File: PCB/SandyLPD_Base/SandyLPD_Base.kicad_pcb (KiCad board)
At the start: 2 copper layers, 270.8 x 100.7 mm, 292 parts, among them J1 Conn_02x02_Odd_Even, J10 Conn_01x10_Pin, J11 Conn_01x03, J12 Conn_01x01_Pin, J2 Conn_01x03, J3 Conn_01x01_Pin, J4 Conn_01x10_Pin, J5 USB_C_Receptacle_USB2.0, J6 USB_C_Receptacle_USB2.0, J7 USB_C_Receptacle_USB2.0, J8 USB_C_Receptacle_USB2.0, J9 Conn_02x02_Odd_Even, SW1 BOOT, SW2 BOOT_ALT, SW3 SW_DIP_x04, SW4 BOOT, SW5 BOOT_ALT, SW6 SW_DIP_x04, U1 NCP1117-3.3_SOT223, U2 NCP1117-3.3_SOT223, U3 RP2040, U4 W25Q128JVPIQ, U5 RP2040, U6 W25Q128JVPIQ, Y1 12MHz, Y2 12MHz

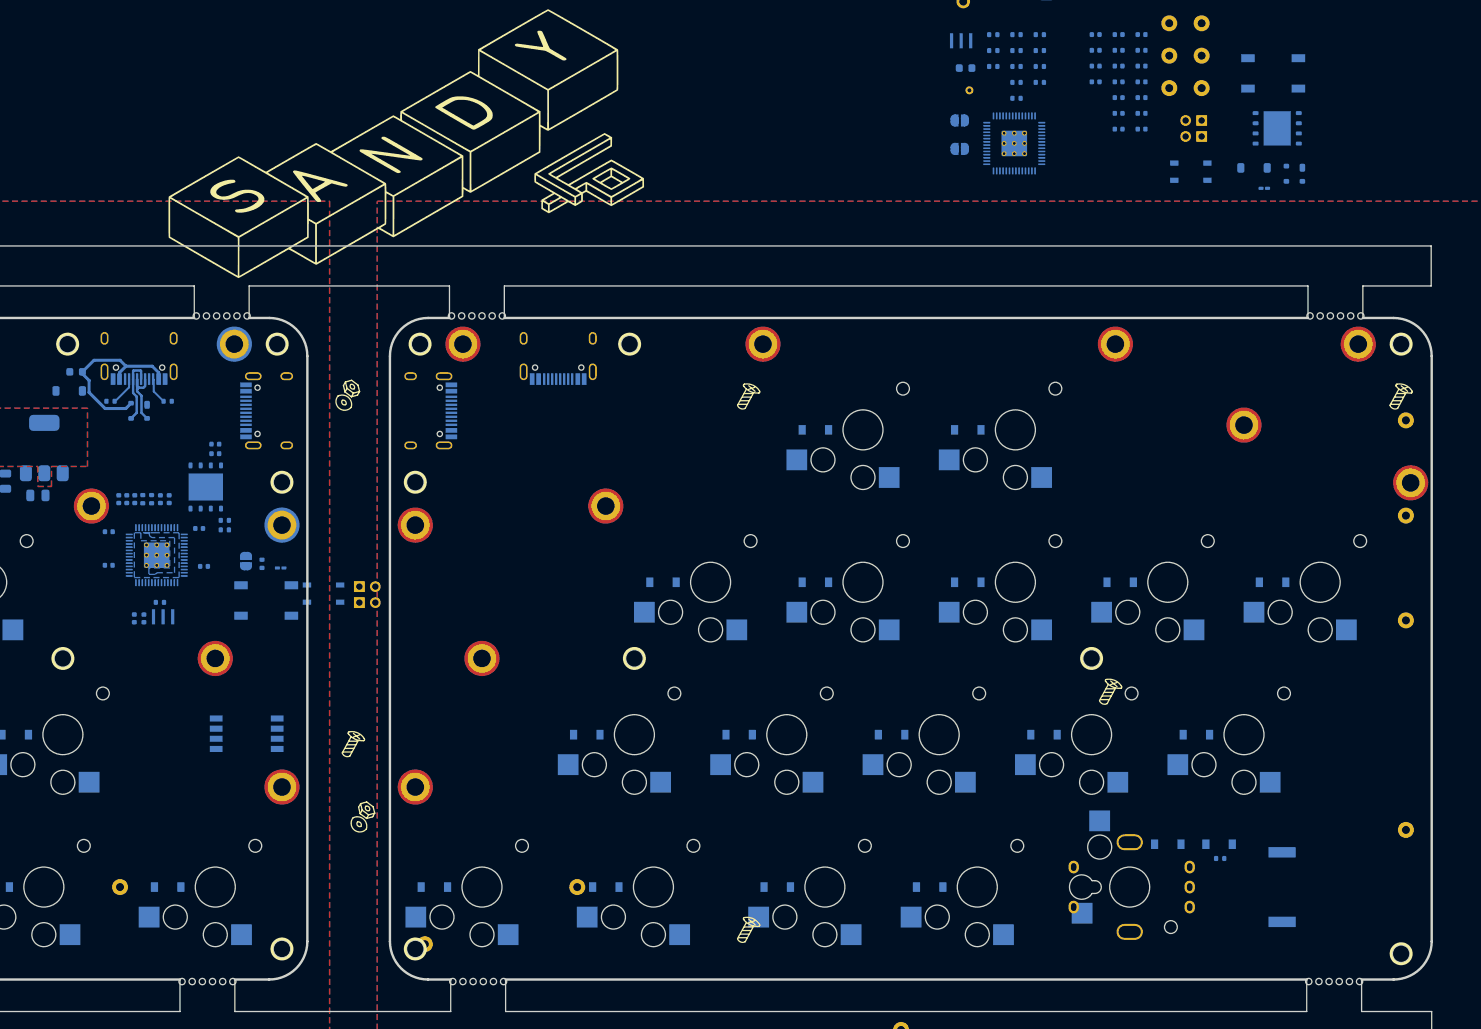
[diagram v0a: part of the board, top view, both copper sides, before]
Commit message: Base基板 MCUまわりの配置検討
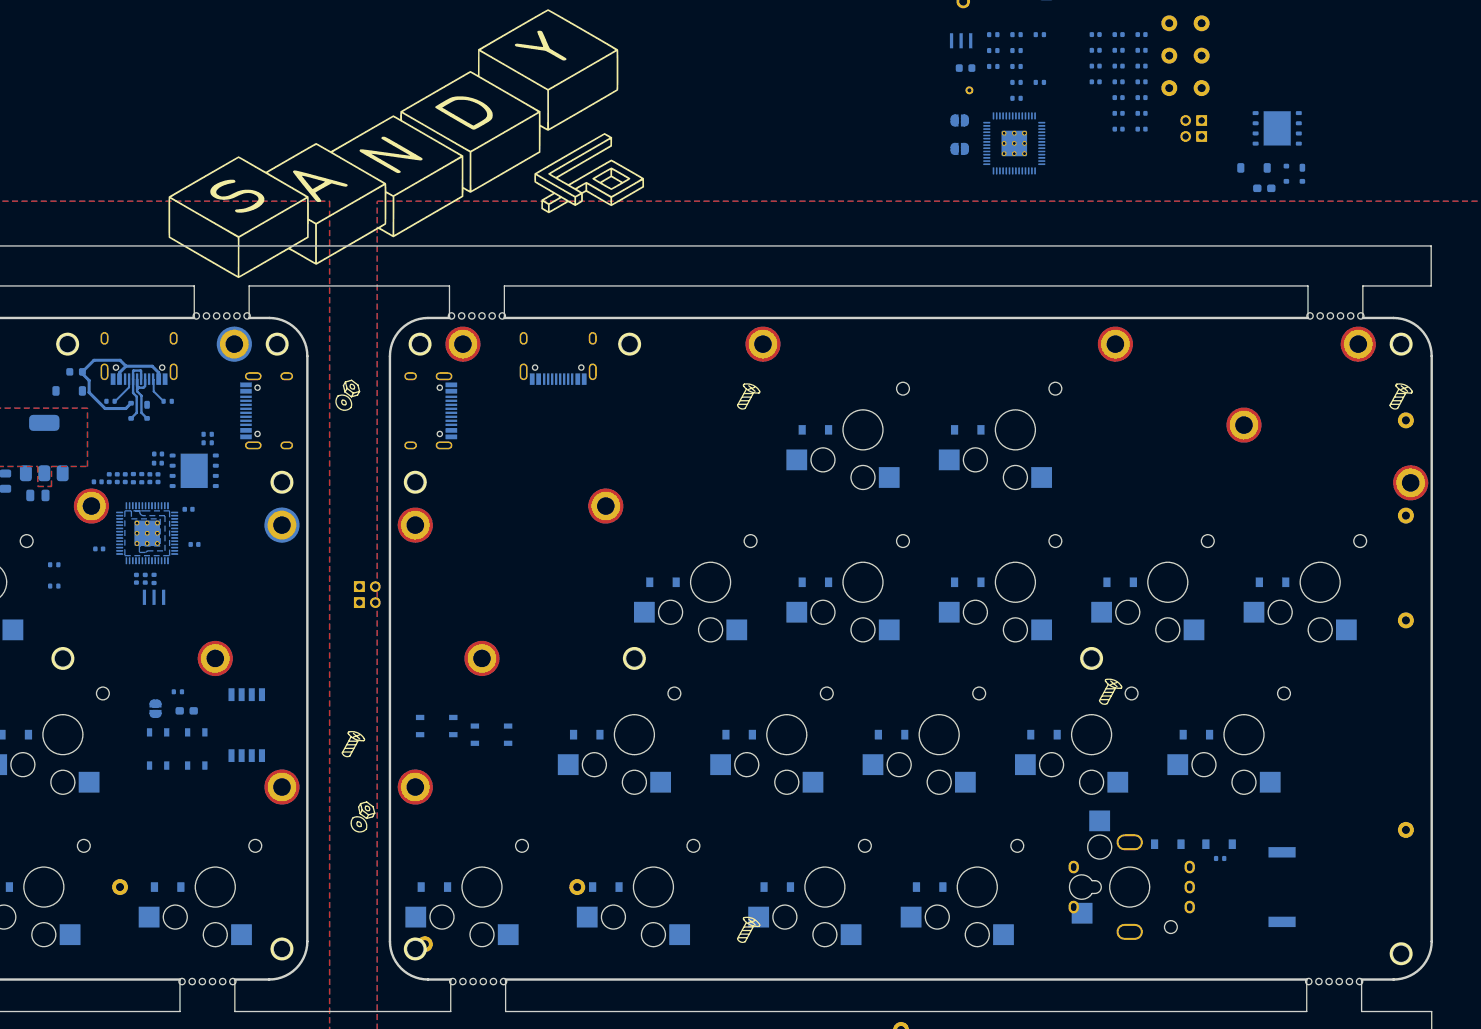
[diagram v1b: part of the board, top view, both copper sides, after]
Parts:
- removed the SW1 at (148.9, 67.4)
- removed the SW4 at (274.7, 1.49)
- added SW2: RESET_ALT, Button_Switch_SMD:SW_SPST_PTS810, B.Cu at (135.4, 85.9)
- added SW5: RESET_ALT, Button_Switch_SMD:SW_SPST_PTS810, B.Cu at (170.2, 83.1)
- STLED1, STLED2: footprint LED_SMD:LED_0201_0603Metric_Pad0.64x0.40mm_HandSolder -> LED_SMD:LED_0603_1608Metric_Pad1.05x0.95mm_HandSolder
- moved R8 140.2 mm to (122.4, 65.6)
- moved R12 138.0 mm to (122.4, 62.9)
- moved SW4 112.2 mm to (177.0, 84.2)
- moved REF** 76.6 mm to (111.0, 26.4)
- moved REF** 76.6 mm to (110.6, 24.6)
- moved REF** 64.5 mm to (121.1, 24.6)
- moved REF** 64.5 mm to (121.6, 26.2)
- moved SW1 25.1 mm to (140.1, 85.9), turned to -90 degrees
- moved JP1 21.6 mm to (135.0, 80.9)
- moved STLED1 21.4 mm to (138.9, 81.2)
- moved R1 19.1 mm to (137.8, 78.8), turned to 180 degrees
- moved REF** 14.0 mm to (159.8, 80.6)
- moved REF** 14.0 mm to (159.4, 78.8)
- moved R5 12.1 mm to (141.5, 46.6), turned to 0 degrees
- moved R4 9.93 mm to (141.5, 47.7), turned to 0 degrees
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- renumbered SW2 to SW1, SW5 to SW4
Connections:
- C7 pad 1: (no net) -> +3V3
- C7 pad 2: (no net) -> GND

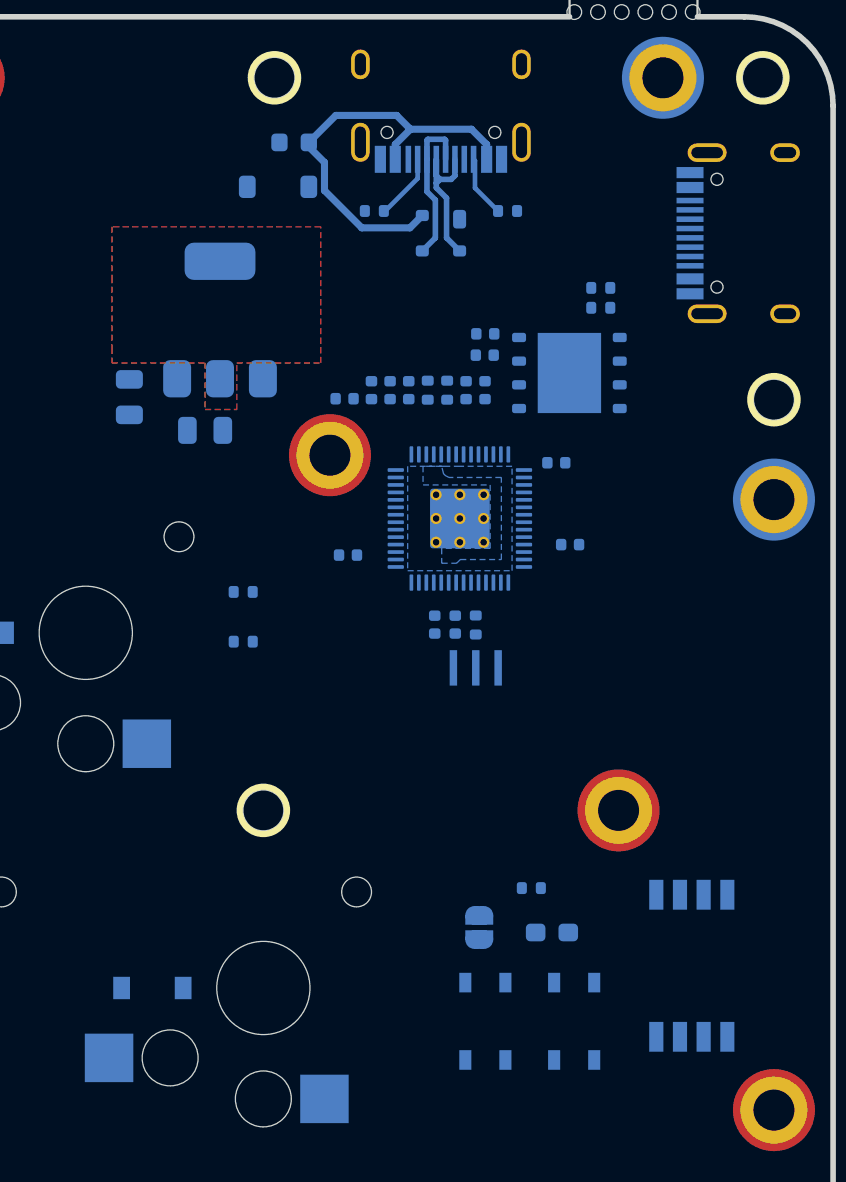
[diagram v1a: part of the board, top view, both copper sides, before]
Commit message: Base基板 MCUまわりの配置検討
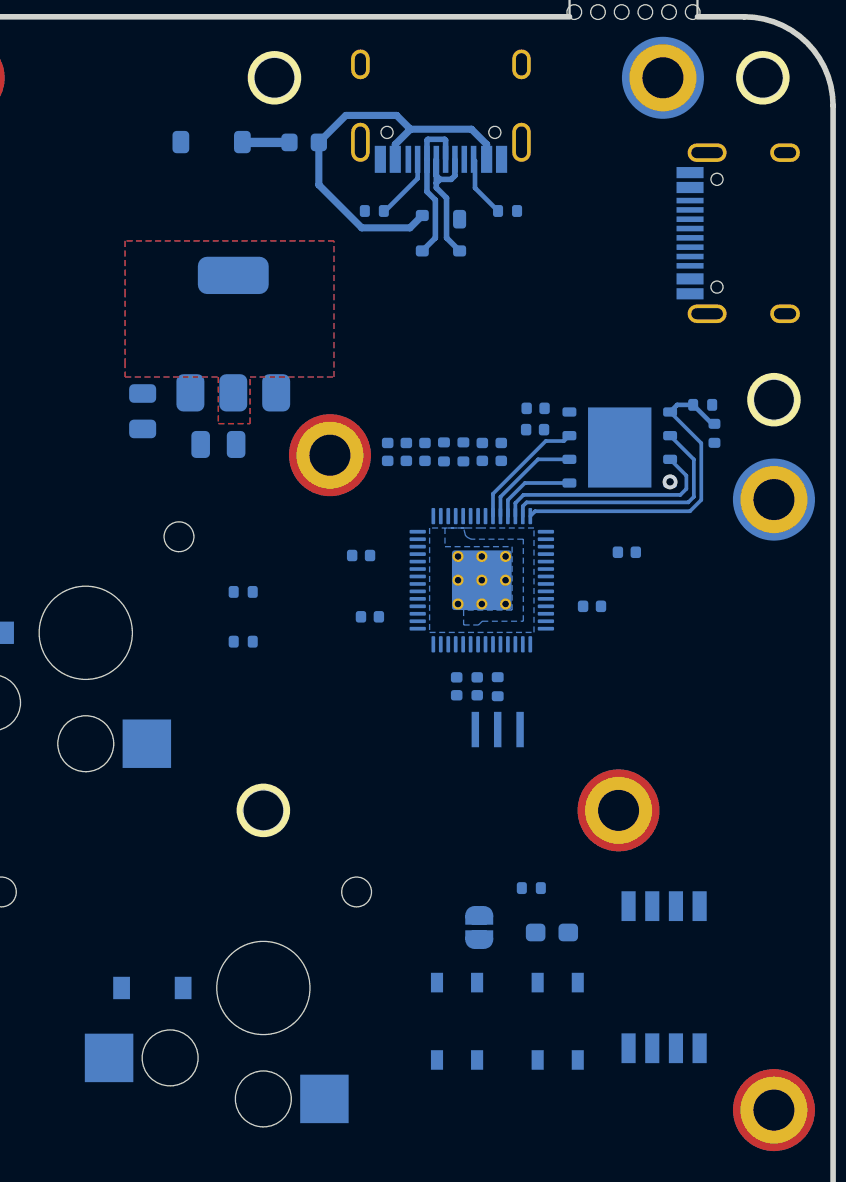
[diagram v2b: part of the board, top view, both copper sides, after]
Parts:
- moved R5 9.90 mm to (147.6, 54.4), turned to 90 degrees
- moved C7 8.46 mm to (128.7, 61.0)
- moved R4 7.55 mm to (147.0, 52.9), turned to 180 degrees
- moved C11 6.11 mm to (142.9, 60.8)
- moved C12 4.82 mm to (138.0, 54.2)
- moved C13 4.82 mm to (138.1, 53.1)
- moved U4 4.82 mm to (142.6, 55.2)
- moved SD1 4.30 mm to (120.7, 38.8)
- moved C6 3.51 mm to (134.9, 68.0)
- moved C8 3.51 mm to (129.2, 64.2)
- moved C10 3.51 mm to (141.1, 63.7)
- moved C4 3.51 mm to (133.8, 68.0)
- moved U3 3.51 mm to (135.2, 62.3)
- moved R6 3.51 mm to (136.0, 68.0)
- moved Y1 3.51 mm to (136.0, 70.3)
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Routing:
- net L_QSPI_SS: track 0.00 -> 17.9 mm
- net L_QSPI_SD1: track 0.00 -> 13.7 mm
- net L_QSPI_SD2: track 0.00 -> 12.1 mm
- net L_QSPI_SD3: track 0.00 -> 6.59 mm
- net L_QSPI_SCLK: track 0.00 -> 5.56 mm
- net L_QSPI_SD0: track 0.00 -> 4.54 mm
- net Net-(SD1-A): track 0.00 -> 2.53 mm
- net VBUS: track 22.8 -> 22.1 mm
- net GND: track 0.00 -> 0.06 mm, vias 0 -> 1

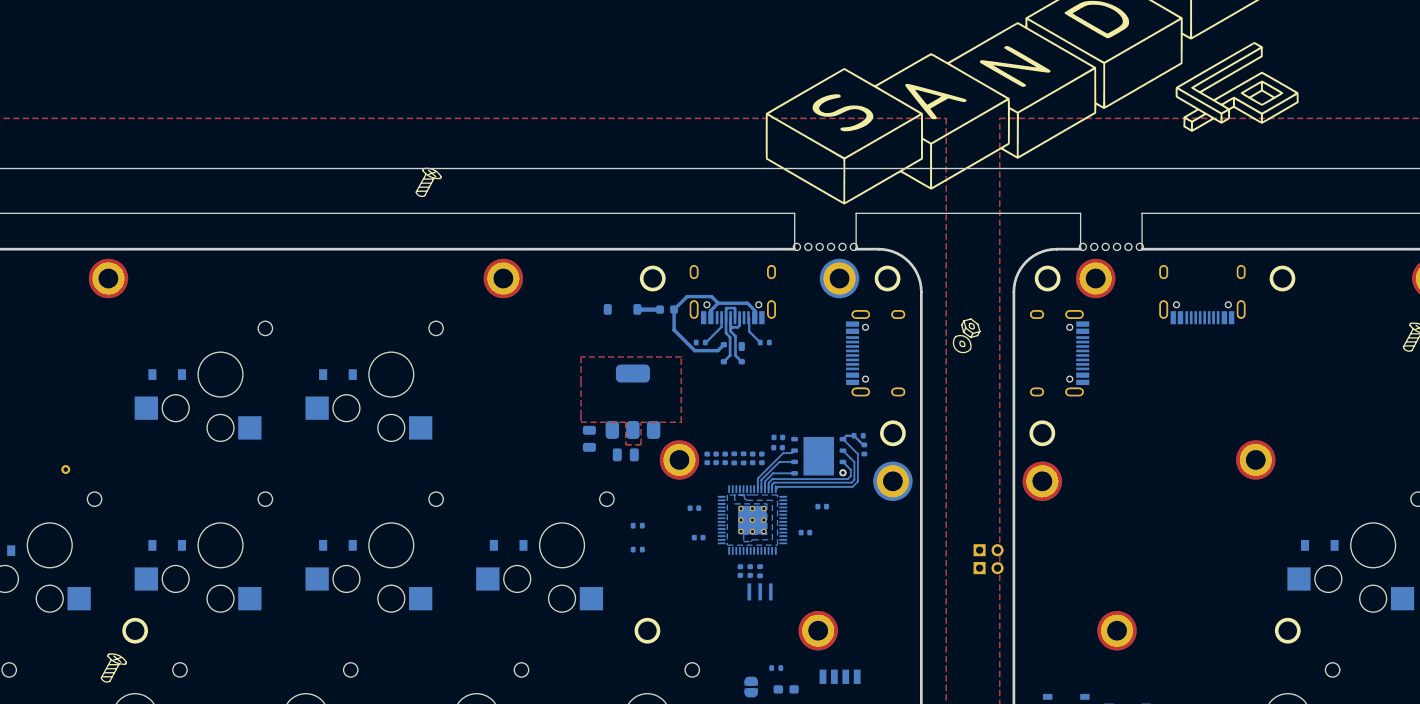
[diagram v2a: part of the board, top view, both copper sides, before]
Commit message: ネジ位置調整中
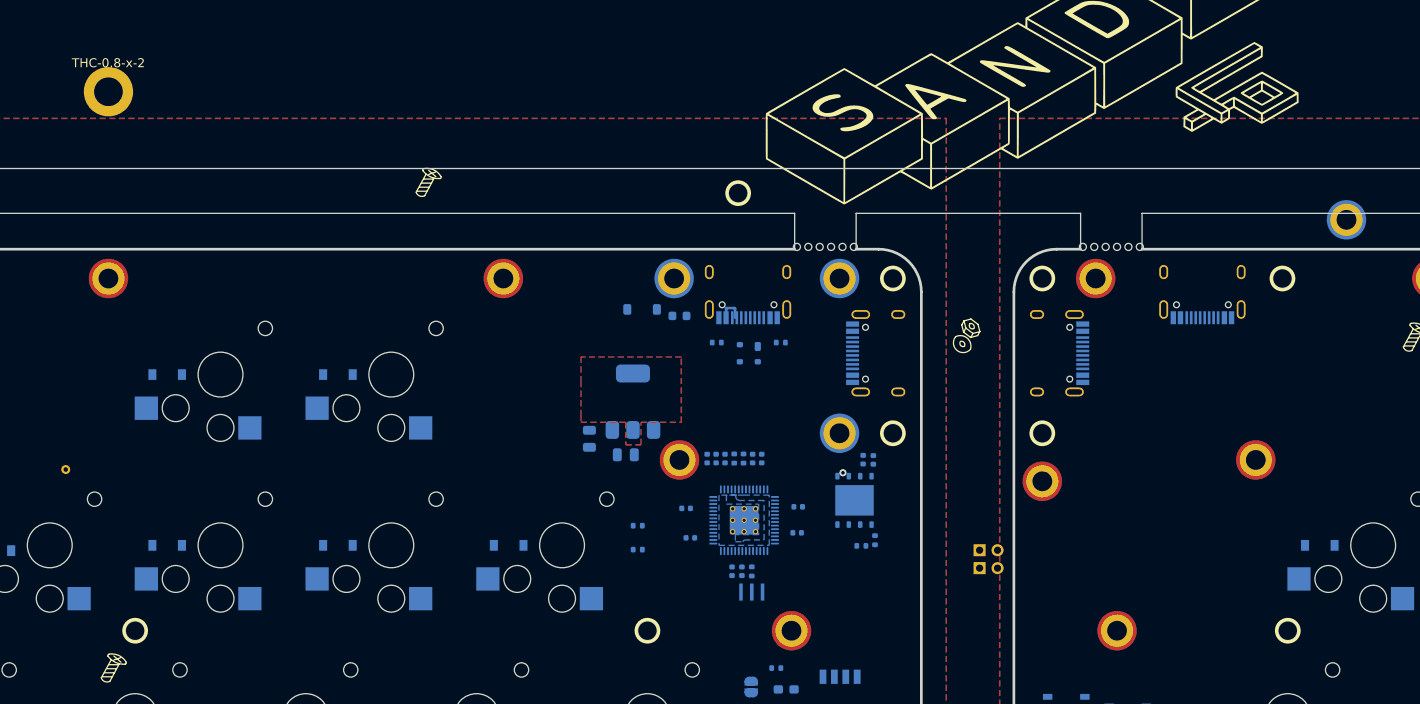
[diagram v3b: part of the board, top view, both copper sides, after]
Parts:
- added H_mid_21: MountingHole, locallib:MountingHole_1.8-2.2mm_M2_Pad_minimal, F.Cu at (126.4, 35.3)
- added H_mid_22: MountingHole, locallib:MountingHole_1.8-2.2mm_M2_Pad_minimal, F.Cu at (201.4, 28.8)
- added THC-0.8-x-2: MountingHole_2.2mm_M2_Pad_TopBottom, MountingHole:MountingHole_2.2mm_M2_Pad_TopBottom, F.Cu at (63.3, 14.5)
- moved H_btm_6 13.5 mm to (133.6, 25.8)
- moved R4 11.8 mm to (148.8, 64.5), turned to 90 degrees
- moved C13 10.9 mm to (148.7, 55.6), turned to 90 degrees
- moved R5 10.8 mm to (147.3, 65.2), turned to 0 degrees
- moved C12 9.58 mm to (147.5, 55.5), turned to 90 degrees
- moved H_mid_20 8.01 mm to (144.9, 52.6)
- moved U4 6.33 mm to (146.6, 60.1), turned to 90 degrees
- moved H_mid_15 2.98 mm to (139.5, 74.6)
- moved C11 2.68 mm to (140.3, 60.8)
- moved SD1 2.18 mm to (122.9, 38.8)
- moved D36 1.79 mm to (134.8, 43.7)
- moved R10 1.79 mm to (131.2, 42.5)
- moved R11 1.79 mm to (138.3, 42.5)
- moved J5 1.70 mm to (134.7, 35.7)
- moved F1 1.55 mm to (127.0, 39.5)
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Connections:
- H_mid_10 pad 1: L_col4 -> L_row1
- H_mid_11 pad 1: R_row1 -> R_col5
- H_mid_12 pad 1: R_col4 -> R_row1
- H_mid_19 pad 1: L_col5 -> GND
- H_mid_20 pad 1: L_row1 -> L_col5
- H_mid_3 pad 1: L_row0 -> L_col4
- H_mid_4 pad 1: R_col5 -> GND_R
- H_mid_5 pad 1: R_row0 -> R_col4
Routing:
- net VBUS: track 22.1 -> 0.00 mm
- net L_QSPI_SS: track 17.9 -> 0.00 mm
- net L_QSPI_SD1: track 13.7 -> 0.00 mm
- net L_QSPI_SD2: track 12.1 -> 0.00 mm
- net L_D+: track 8.63 -> 0.00 mm
- net L_QSPI_SD3: track 6.59 -> 0.00 mm
- net L_QSPI_SCLK: track 5.56 -> 0.00 mm
- net L_D-: track 8.48 -> 3.09 mm
- net L_QSPI_SD0: track 4.54 -> 0.06 mm, vias 0 -> 1
- net Net-(J5-CC1): track 3.56 -> 0.00 mm
- net Net-(J5-CC2): track 3.31 -> 0.00 mm
- net Net-(SD1-A): track 2.53 -> 0.00 mm
- net GND: track 0.06 -> 0.00 mm, vias 1 -> 0
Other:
- board text added: "2024.12.17 Midのネジ穴位置（Mid→Topネジ穴位置も同一）決定ずみ Topプレート用ネジ穴決定ずみ（User.Eco2) ToDo Base→ボトムプレートのネジ穴をMidと共通化して、不要分を消す。 Midのネジ穴すべてをボトムに繋げる必要なし（四隅プラスアルファでよい）"
- board text added: "Screw for Top plate"
